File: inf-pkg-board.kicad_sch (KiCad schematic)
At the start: 60 parts, among them J1 stemmaQT, J2 Conn_01x01_Pin, J3 Conn_01x01_Pin, J4 SWD, J5 USB_C_Receptacle_USB2.0_14P, J6 ePaper Hat, Q1 2N7002, U1 ME6211C33M5, U2 W25Q128JVS, U3 RP2040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

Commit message: fixes
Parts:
- removed U1: ME6211C33M5, Package_TO_SOT_SMD:SOT-23-5, symbol Regulator_Linear:ME6211C33M5
- added C22: 100n, Capacitor_SMD:C_0402_1005Metric, symbol Device:C
- added C23, C24: 100p, Capacitor_SMD:C_0402_1005Metric, symbol Device:C_Small
- added D2, D3: LED, Diode_SMD:D_0805_2012Metric, symbol Device:LED
- added J7, J8: Conn_01x01_Pin, Connector_PinHeader_1.00mm:PinHeader_1x01_P1.00mm_Vertical, symbol Connector:Conn_01x01_Pin
- added JP4: Jumper_2_Small_Bridged, Jumper:SolderJumper-2_P1.3mm_Bridged_Pad1.0x1.5mm, symbol Jumper:Jumper_2_Small_Bridged
- added Q2: AO3400A, Package_TO_SOT_SMD:SOT-23, symbol Transistor_FET:2N7002
- added R14, R16, R17: 330, Resistor_SMD:R_0402_1005Metric, symbol Device:R
- added R15: 5.1k, Resistor_SMD:R_0402_1005Metric, symbol Device:R_Small
- added R2: 27, Resistor_SMD:R_0402_1005Metric, symbol Device:R
- added U7: SPX3819M5-L-3-3, Package_TO_SOT_SMD:SOT-23-5, symbol Regulator_Linear:SPX3819M5-L-3-3
- H1, H2, H3, H4, J2, J3, JP1, JP2, JP3, TP1: now not fitted; now left out of the parts list
- L1: footprint Inductor_SMD:L_0201_0603Metric -> Inductor_SMD:L_0402_1005Metric; LCSC (none) -> C27149
- Q1: value 2N7002 -> AO3400A; LCSC C8545 -> C20917
- R1, R13, R3, R5, R6: footprint Capacitor_SMD:C_0402_1005Metric -> Resistor_SMD:R_0402_1005Metric
- R12: value 10k -> 1M; footprint Resistor_SMD:R_0805_2012Metric -> Resistor_SMD:R_0402_1005Metric; LCSC C17414 -> C26083
- R4: footprint Resistor_SMD:R_0402_1005Metric -> Resistor_SMD:R_0805_2012Metric; LCSC C25744 -> C17414
- U4: LCSC (none) -> C3019759
- U6: LCSC (none) -> C558418
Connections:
- net +3V3: now also C24.2, U7.5 (OUT)
- net 32kHz: now also R2.1; no longer U4.1 (CLKOUT)
- net CC_GND: now also JP4.1 (A), Q2.3 (D); no longer U4.2 (~{INT})
- net GND: now also C22.2, C24.1, JP4.2 (B), R14.2, R15.1, R16.2, R17.1, U7.2 (GND); no longer R12.2
- net VBUS: now also U7.1 (IN), U7.3 (EN)
- net at U3.13 (GPIO10): now also D2.2 (A)
- net at U3.14 (GPIO11): now also D3.2 (A)
- net at U3.17 (GPIO14): now also J8.1 (Pin_1)
- net at U3.18 (GPIO15): now also J7.1 (Pin_1)
- net at U5.2 (FMI): now also C23.2; no longer J3.1 (Pin_1)
- net at TP1.1, U5.6 (~{SEN}): now also R15.2
- net at C20.2, U4.6 (VBACKUP): now also R12.1, Q2.1 (G)
- net at D1.1 (K): now also R14.1; no longer R12.1
- new net: D2.1 (K), R17.2
- new net: R2.2, U4.1 (CLKOUT)
- new net: D3.1 (K), R16.1
- new net: Q2.2 (S), R12.2, U4.2 (~{INT})
- new net: C22.1, U7.4 (BP)
- new net: C23.1, J3.1 (Pin_1)
- no-connect marks 27 -> 23
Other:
- moved on the sheet: L1

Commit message: fix bom error / add debug pads
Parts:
- added J9: Conn_ARM_SWD_TagConnect_TC2030, Connector:Tag-Connect_TC2030-IDC-FP_2x03_P1.27mm_Vertical, symbol Connector:Conn_ARM_SWD_TagConnect_TC2030
- added TP_CC_LATCH1, TP_CLK1, TP_GND1, TP_INT1: TestPoint, TestPoint:TestPoint_Pad_D1.5mm, symbol Connector:TestPoint
- added TP_V33: 3.3V_TEST, TestPoint:TestPoint_Pad_D2.0mm, symbol Connector:TestPoint
- added TP_VB1: VBUS_TEST, TestPoint:TestPoint_Pad_D2.0mm, symbol Connector:TestPoint
- C1, C2: LCSC C52923 -> C1557
- C10, C17, C18, C19, C8: LCSC C307331 -> C52923
- C11, C12, C13, C14, C15, C16, C21, C22, C4, C6, C7, C9: LCSC C126504 -> C1525
- J4: footprint Connector_PinHeader_1.27mm:PinHeader_2x05_P1.27mm_Vertical -> Connector_PinHeader_1.27mm:PinHeader_2x05_P1.27mm_Vertical_SMD
- U6: LCSC C558418 -> C85364
- U7: LCSC (none) -> C9055
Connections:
- net +3V3: now also J9.1 (VCC), TP_V33.1
- net 32kHz: now also TP_CLK1.1
- net GND: now also J9.5 (GND), TP_GND1.1
- net RUN: now also J9.3 (~{RESET})
- net SWCLK: now also J9.4 (SWCLK)
- net SWD: now also J9.2 (SWDIO)
- net VBUS: now also TP_VB1.1
- net at Q1.1 (G), R7.2, U3.31 (GPIO20): now also TP_CC_LATCH1.1
- net at Q2.2 (S), R12.2, U4.2 (~{INT}): now also TP_INT1.1
- no-connect marks 23 -> 24
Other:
- moved on the sheet: J1

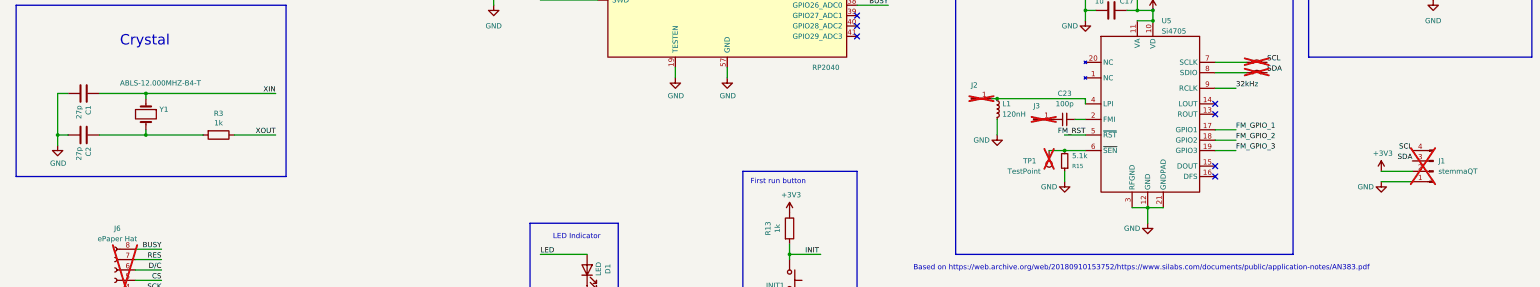
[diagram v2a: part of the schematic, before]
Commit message: bom optimization
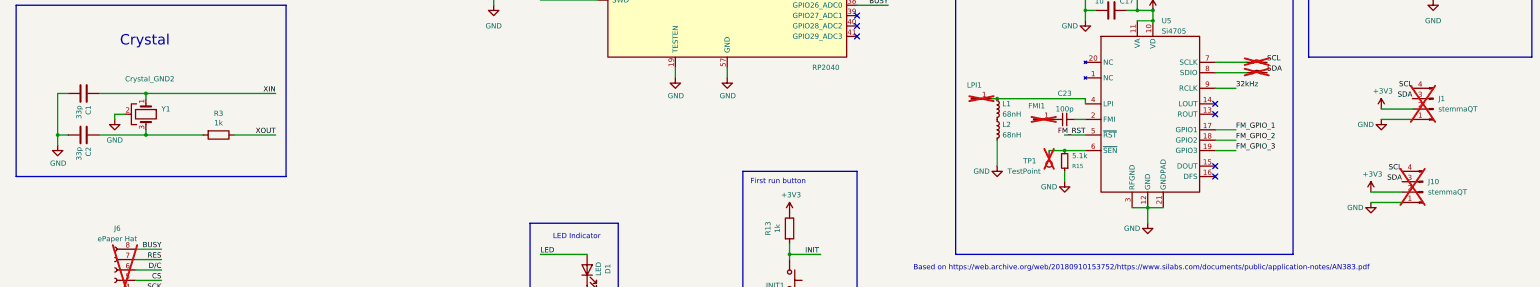
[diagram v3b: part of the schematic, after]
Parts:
- removed Y1: ABLS-12.000MHZ-B4-T, RP2040_minimal:Crystal_SMD_HC49-US, symbol Device:Crystal
- added J10: stemmaQT, Connector_JST:JST_PH_B4B-PH-K_1x04_P2.00mm_Vertical, symbol Connector:Conn_01x04_Pin
- added L2: 68nH, Inductor_SMD:L_0603_1608Metric, symbol Device:L_Small
- added Y1: Crystal_GND2, Crystal:Crystal_SMD_3225-4Pin_3.2x2.5mm, symbol Device:Crystal_GND2
- C1, C2: value 27p -> 33p; LCSC C1557 -> C1562
- L1: value 120nH -> 68nH; footprint Inductor_SMD:L_0402_1005Metric -> Inductor_SMD:L_0603_1608Metric; LCSC C27149 -> C13415
- R5, R6: footprint Resistor_SMD:R_0402_1005Metric -> Resistor_SMD:R_0603_1608Metric; LCSC C274349 -> C25190
- renumbered J3 to FMI1, J2 to LPI1
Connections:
- net +3V3: now also J10.2 (Pin_2)
- net GND: now also J10.1 (Pin_1), L2.2, Y1.2; no longer L1.2
- net SCL: now also J10.4 (Pin_4)
- net SDA: now also J10.3 (Pin_3)
- net XIN: now also Y1.1
- net at C2.1, R3.2: now also Y1.3
- new net: L1.2, L2.1
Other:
- moved on the sheet: J1

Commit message: final tweaks
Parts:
- added R18: 0, Resistor_SMD:R_1206_3216Metric_Pad1.30x1.75mm_HandSolder, symbol Device:R_Small
- J10: value stemmaQT -> stemma
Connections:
- net GND: now also U4.8 (EVI)
- net at Q2.1 (G), R12.1, U4.6 (VBACKUP): now also R18.2; no longer C20.2
- new net: C20.2, R18.1
- no-connect marks 24 -> 23
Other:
- moved on the sheet: C20
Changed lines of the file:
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@@
 	)
 	(no_connect
-		(at 279.4 142.24)
-	)
-	(no_connect
 		(at 229.87 132.08)
 	)
@@
 	(wire
 		(pts
+			(xy 274.32 143.51) (xy 274.32 142.24)
+		)
+		(stroke
+			(width 0)
+			(type default)
+		)
+	)
+	(wire
+		(pts
 			(xy 223.52 60.96) (xy 234.95 60.96)
 		)
@@
 	(wire
 		(pts
+			(xy 274.32 142.24) (xy 279.4 142.24)
+		)
+		(stroke
+			(width 0)
+			(type default)
+		)
+	)
+	(wire
+		(pts
 			(xy 62.23 31.75) (xy 67.31 31.75)
 		)
@@
 	(wire
 		(pts
-			(xy 298.45 119.38) (xy 309.88 119.38)
+			(xy 298.45 114.3) (xy 309.88 114.3)
 		)
 		(stroke
@@
 	(symbol
 		(lib_id "Device:C")
-		(at 298.45 123.19 0)
+		(at 298.45 118.11 0)
 		(unit 1)
 		(exclude_from_sim no)
@@
 		(fields_autoplaced yes)
 		(property "Reference" "C20"
-			(at 302.26 121.9199 0)
+			(at 302.26 116.8399 0)
 			(effects
 				(font
@@
 		)
 		(property "Value" "C"
-			(at 302.26 124.4599 0)
+			(at 302.26 119.3799 0)
 			(effects
 				(font
@@
 		)
 		(property "Footprint" "Capacitor_THT:C_R21.00mm_P6.00mm"
-			(at 299.4152 127 0)
+			(at 299.4152 121.92 0)
 			(effects
 				(font
@@
 		)
 		(property "Datasheet" "~"
-			(at 298.45 123.19 0)
+			(at 298.45 118.11 0)
 			(effects
 				(font
@@
 		)
 		(property "Description" "Unpolarized capacitor"
-			(at 298.45 123.19 0)
+			(at 298.45 118.11 0)
 			(effects
 				(font
@@
 		(lib_name "GND_6")
 		(lib_id "power:GND")
-		(at 309.88 119.38 0)
+		(at 309.88 114.3 0)
 		(unit 1)
 		(exclude_from_sim no)
@@
 		(fields_autoplaced yes)
 		(property "Reference" "#PWR025"
-			(at 309.88 125.73 0)
+			(at 309.88 120.65 0)
 			(effects
 				(font
@@
 		)
 		(property "Value" "GND"
-			(at 309.88 124.46 0)
+			(at 309.88 119.38 0)
 			(effects
 				(font
@@
 		)
 		(property "Footprint" ""
-			(at 309.88 119.38 0)
+			(at 309.88 114.3 0)
 			(effects
 				(font
@@
 		)
 		(property "Datasheet" ""
-			(at 309.88 119.38 0)
+			(at 309.88 114.3 0)
 			(effects
 				(font
@@
 		)
 		(property "Description" "Power symbol creates a global label with name \"GND\" , ground"
-			(at 309.88 119.38 0)
+			(at 309.88 114.3 0)
 			(effects
 				(font
@@
 	)
 	(symbol
+		(lib_name "GND_10")
+		(lib_id "power:GND")
+		(at 274.32 143.51 0)
+		(unit 1)
+		(exclude_from_sim no)
+		(in_bom yes)
+		(on_board yes)
+		(dnp no)
+		(fields_autoplaced yes)
+		(property "Reference" "#PWR056"
+			(at 274.32 149.86 0)
+			(effects
+				(font
+					(size 1.27 1.27)
+				)
+				(hide yes)
+			)
+		)
+		(property "Value" "GND"
+			(at 274.32 148.59 0)
+			(effects
+				(font
+					(size 1.27 1.27)
+				)
+			)
+		)
+		(property "Footprint" ""
+			(at 274.32 143.51 0)
+			(effects
+				(font
+					(size 1.27 1.27)
+				)
+				(hide yes)
+			)
+		)
+		(property "Datasheet" ""
+			(at 274.32 143.51 0)
+			(effects
+				(font
+					(size 1.27 1.27)
+				)
+				(hide yes)
+			)
+		)
+		(property "Description" "Power symbol creates a global label with name \"GND\" , ground"
+			(at 274.32 143.51 0)
+			(effects
+				(font
+					(size 1.27 1.27)
+				)
+				(hide yes)
+			)
+		)
+		(pin "1"
+		)
+		(instances
+			(project ""
+				(path "/0b572f4d-42c2-4e67-a259-3bf815f1855a"
+					(reference "#PWR056")
+					(unit 1)
+				)
+			)
+		)
+	)
+	(symbol
 		(lib_id "Connector:Conn_ARM_SWD_TagConnect_TC2030")
 		(at 373.38 168.91 0)
@@
 	)
 	(symbol
+		(lib_id "Device:R_Small")
+		(at 298.45 124.46 0)
+		(unit 1)
+		(exclude_from_sim no)
+		(in_bom yes)
+		(on_board yes)
+		(dnp no)
+		(fields_autoplaced yes)
+		(property "Reference" "R18"
+			(at 300.99 123.1899 0)
+			(effects
+				(font
+					(size 1.016 1.016)
+				)
+				(justify left)
+			)
+		)
+		(property "Value" "0"
+			(at 300.99 125.7299 0)
+			(effects
+				(font
+					(size 1.27 1.27)
+				)
+				(justify left)
+			)
+		)
+		(property "Footprint" "Resistor_SMD:R_1206_3216Metric_Pad1.30x1.75mm_HandSolder"
+			(at 298.45 124.46 0)
+			(effects
+				(font
+					(size 1.27 1.27)
+				)
+				(hide yes)
+			)
+		)
+		(property "Datasheet" "~"
+			(at 298.45 124.46 0)
+			(effects
+				(font
+					(size 1.27 1.27)
+				)
+				(hide yes)
+			)
+		)
+		(property "Description" "Resistor, small symbol"
+			(at 298.45 124.46 0)
+			(effects
+				(font
+					(size 1.27 1.27)
+				)
+				(hide yes)
+			)
+		)
+		(property "LCSC" "C17888"
+			(at 298.45 124.46 0)
+			(effects
+				(font
+					(size 1.27 1.27)
+				)
+				(hide yes)
+			)
+		)
+		(pin "1"
+		)
+		(pin "2"
+		)
+		(instances
+			(project ""
+				(path "/0b572f4d-42c2-4e67-a259-3bf815f1855a"
+					(reference "R18")
+					(unit 1)
+				)
+			)
+		)
+	)
+	(symbol
 		(lib_name "GND_9")
 		(lib_id "power:GND")
@@
 			)
 		)
-		(property "Value" "stemmaQT"
+		(property "Value" "stemma"
 			(at 369.57 226.0599 0)
 			(effects

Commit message: swap resistor to smaller/standard size
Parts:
- R2: footprint Resistor_SMD:R_0402_1005Metric -> Resistor_SMD:R_0603_1608Metric; LCSC C274349 -> C25190
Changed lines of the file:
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@@
 			)
 		)
-		(property "Footprint" "Resistor_SMD:R_0402_1005Metric"
+		(property "Footprint" "Resistor_SMD:R_0603_1608Metric"
 			(at 308.61 140.462 90)
 			(effects
@@
 			)
 		)
-		(property "LCSC" "C274349"
+		(property "LCSC" "C25190"
 			(at 308.61 142.24 0)
 			(effects

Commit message: check
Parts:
- removed Q1, Q2: AO3400A, Package_TO_SOT_SMD:SOT-23, symbol Transistor_FET:2N7002
- removed R18: 0, Resistor_SMD:R_1206_3216Metric_Pad1.30x1.75mm_HandSolder, symbol Device:R_Small
- removed R7: 1M, Resistor_SMD:R_0402_1005Metric, symbol Device:R_Small
- added C25, C26: 100n, Capacitor_SMD:C_0402_1005Metric, symbol Device:C
- added C27: C, Capacitor_THT:C_Disc_D16.0mm_W5.0mm_P10.00mm, symbol Device:C
- added R7: 100k, Resistor_SMD:R_0402_1005Metric, symbol Device:R
- added TP_SCAP: TestPoint, TestPoint:TestPoint_Pad_D2.5mm, symbol Connector:TestPoint
- added TP_V33_2: 3.3V_TEST, TestPoint:TestPoint_Pad_D2.0mm, symbol Connector:TestPoint
- added U1, U8: 74LVC1G07, Package_TO_SOT_SMD:SOT-353_SC-70-5, symbol 74xGxx:74LVC1G07
- J7, J8, LPI1: footprint Connector_PinHeader_1.00mm:PinHeader_1x01_P1.00mm_Vertical -> Connector_PinHeader_2.54mm:PinHeader_1x01_P2.54mm_Vertical
- JP4: footprint Jumper:SolderJumper-2_P1.3mm_Bridged_Pad1.0x1.5mm -> Jumper:SolderJumper-2_P1.3mm_Open_TrianglePad1.0x1.5mm
- R12: value 1M -> 100k; LCSC C26083 -> C25741
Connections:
- net +3V3: now also C25.1, R7.1, TP_V33_2.1, U8.5 (VCC)
- net CC_GND: now also U1.4, U8.4
- net GND: now also C25.2, C26.2, C27.1, U1.3 (GND), U8.3 (GND)
- net CC_LATCH: now reaches TP_CC_LATCH1.1, U3.31 (GPIO20)
- net CC_LATCH: now also R7.2, U8.2
- net S_CAP: now reaches C20.2
- net S_CAP: now also R12.1, U4.6 (VBACKUP), C26.1, C27.2, TP_SCAP.1, U1.5 (VCC)
- net CLK_INT: now reaches R12.2, TP_INT1.1, U4.2 (~{INT})
- net CLK_INT: now also U1.2
- no-connect marks 23 -> 25
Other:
- moved on the sheet: JP3, R8, R9

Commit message: fixes
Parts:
- C27: now not fitted; now left out of the parts list
- renumbered TP_SCAP to TP_SCAP1
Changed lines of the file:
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@@
 		(on_board yes)
 		(dnp no)
-		(property "Reference" "TP_SCAP"
+		(property "Reference" "TP_SCAP1"
 			(at 299.72 123.952 90)
 			(effects
@@
 			(project ""
 				(path "/0b572f4d-42c2-4e67-a259-3bf815f1855a"
-					(reference "TP_SCAP")
+					(reference "TP_SCAP1")
 					(unit 1)
 				)
@@
 		(unit 1)
 		(exclude_from_sim no)
-		(in_bom yes)
+		(in_bom no)
 		(on_board yes)
-		(dnp no)
+		(dnp yes)
 		(property "Reference" "C27"
 			(at 288.798 115.062 0)
